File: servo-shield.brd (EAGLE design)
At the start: 65 x 56 mm, 30 parts, among them IC1 24AA01P, K1 PIN20X2

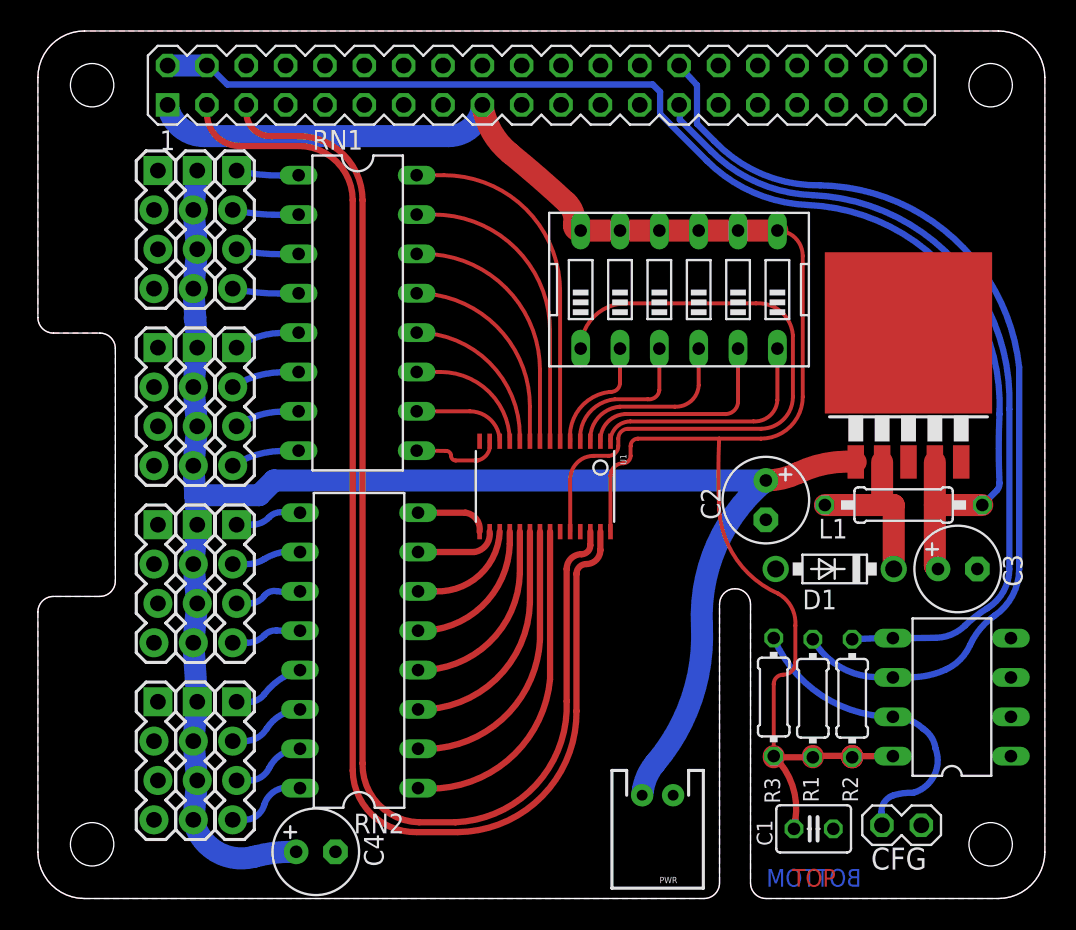
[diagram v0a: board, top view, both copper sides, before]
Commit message: Mk2 board. Move servo connectors to longer edge, remove HAT related crap. We're not using it anyway, its just i2c. Fixed issues with regulator using a bogus inductor. Fixed power connector. Hopefully fixed clearance issues with standoffs. Fixed clearance issue with soldering 40 pin connector hitting previous resistor networks. Use more SMD parts to reduce PCB used space. This WILL require a stencil.
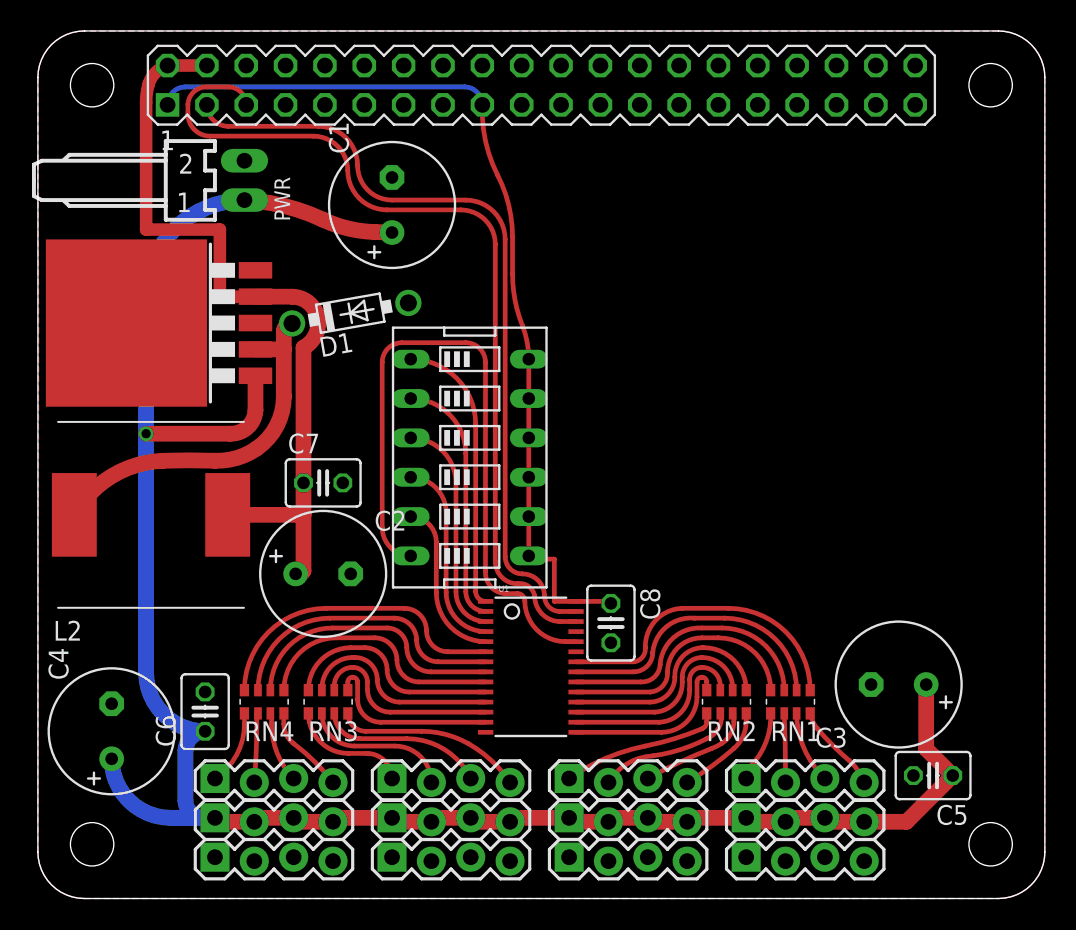
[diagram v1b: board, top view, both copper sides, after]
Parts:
- removed CFG: (no value), FLYFISH:PIN_W_2
- removed IC1: 24AA01P, microchip:DIL8
- removed L1: 33uh, rcl:0207/10
- removed R1, R2: 3k9, rcl:0204/7
- removed R3: 1k, rcl:0204/7
- added C5, C6, C7, C8: 100nf, rcl:C025-030X050
- added L2: 33uh, WE-PD:WE-PD_1260/1245/1280/1210
- added RN3, RN4: (no value), resistor-dil:EXB38V
- C1: value 100nF -> 1000uf; device rcl:C025-030X050 -> rcl:E3,5-8
- C2: value 680uf -> 1000uf; device rcl:E2,5-6 -> rcl:E3,5-8
- C3: value 220uf -> 1000uf; device rcl:E2,5-6 -> rcl:E3,5-8
- C4: value 640uf -> 1000uf; device rcl:E2,5-6 -> rcl:E3,5-8
- PWR: value (none) -> 22-05-7028-02; device SparkFun-Connectors:JST-2-PTH -> con-molex:7395-02
- RN1, RN2: device resistor-dil:DIL16 -> resistor-dil:EXB38V
- moved C1 48.6 mm to (22.9, 44.8), turned to 90 degrees
- moved IC2 48.0 mm to (8.26, 37.1), turned to 90 degrees
- moved PWR 47.8 mm to (13.3, 46.4), turned to 270 degrees
- moved JP9 44.6 mm to (11.4, 2.54), turned to 0 degrees
- moved JP5 41.9 mm to (11.4, 5.08), turned to 0 degrees
- moved JP12 39.4 mm to (45.7, 2.54), turned to 0 degrees
- moved JP1 39.4 mm to (11.4, 7.62), turned to 0 degrees
- moved RN1 37.6 mm to (48.6, 12.7), turned to 180 degrees
- moved JP10 36.4 mm to (22.9, 2.54), turned to 0 degrees
- moved JP8 36.4 mm to (45.7, 5.08), turned to 0 degrees
- moved D1 35.4 mm to (20.2, 37.8), turned to 10 degrees
- moved JP11 34.3 mm to (34.3, 2.54), turned to 0 degrees
- moved JP4 33.4 mm to (45.7, 7.62), turned to 0 degrees
- moved JP6 33.0 mm to (22.9, 5.08), turned to 0 degrees
- moved JP7 30.7 mm to (34.3, 5.08), turned to 0 degrees
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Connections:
- removed net N$16: SW1.6, U1.1
- removed net N$40: D1.C, IC2.2, L1.1
- new net VOUT: D1.C, IC2.2, L2.1
- net +3V3: now also C8.1; no longer C1.1, IC1.8, R1.2, R2.2, R3.2
- net +5V: now also C2.+, C7.1, L2.2; no longer C3.+, L1.2
- net GND: now also C1.-, C5.2, C6.2, C7.2, C8.2, PWR.2; no longer C1.2, CFG.2, IC1.1, IC1.2, IC1.3, IC1.4, PWR.1
- net ID_SCL: no longer IC1.6, R1.1
- net ID_SDA: no longer IC1.5, R2.1
- net N$1: now also RN2.3; no longer RN2.7
- net N$10: now also RN2.6; no longer RN2.10
- net N$11: now also U1.1; no longer U1.24
- net N$12: now also U1.2; no longer U1.5
- net N$13: now also SW1.5, U1.5; no longer SW1.3, U1.4
- net N$14: now also SW1.3; no longer SW1.4
- net N$15: now also SW1.4, U1.4; no longer SW1.5, U1.2
- net N$17: now also RN2.7; no longer RN2.11
- net N$18: now also RN2.8; no longer RN2.12
- net N$19: now also RN1.5; no longer RN2.13
- net N$2: now also RN2.4; no longer RN2.8
- net N$20: now also RN1.6; no longer RN2.14
- net N$21: now also RN1.7; no longer RN2.15
- net N$22: now also RN1.8; no longer RN2.16
- net N$23: now also RN1.1; no longer RN2.1
- net N$24: now also RN1.2; no longer RN2.2
- net N$25: now also RN1.3; no longer RN2.3
- net N$26: now also RN1.4; no longer RN2.4
- net N$27: now also RN2.1; no longer RN2.5
- net N$28: now also RN2.2; no longer RN2.6
- net N$29: now also RN3.2; no longer RN1.10
- net N$3: now also RN3.1; no longer RN1.9
- net N$30: now also RN3.3; no longer RN1.11
- net N$31: now also RN3.4; no longer RN1.12
- net N$32: now also RN4.1; no longer RN1.13
- net N$33: now also RN4.2; no longer RN1.14
- net N$34: now also RN4.3; no longer RN1.15
- net N$35: now also RN4.4; no longer RN1.16
- net N$36: now also RN3.5; no longer RN1.5
- net N$37: now also RN3.8; no longer RN1.8
- net N$38: now also RN3.7; no longer RN1.7
- net N$39: now also RN3.6; no longer RN1.6
- net N$4: now also SW1.6, U1.24; no longer CFG.1, IC1.7, R3.1
- net N$5: now also RN4.8; no longer RN1.4
- net N$6: now also RN4.7; no longer RN1.3
- net N$7: now also RN4.6; no longer RN1.2
- net N$8: now also RN4.5; no longer RN1.1
- net N$9: now also RN2.5; no longer RN2.9
- net V+: now also C1.+, C3.+, C5.1, C6.1, PWR.1; no longer C2.+, PWR.2
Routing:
- net ID_SCL: track 61.0 -> 0.00 mm
- net ID_SDA: track 52.2 -> 0.00 mm
- net +3V3: track 110.5 -> 59.1 mm
- net I2C_SDA: track 80.7 -> 49.4 mm
- net +5V: track 80.0 -> 51.5 mm
- net VOUT: track 0.00 -> 23.4 mm
- net N$4: track 19.5 -> 42.2 mm
- net N$11: track 39.9 -> 17.6 mm
- net I2C_SCL: track 76.5 -> 55.8 mm
- net V+: track 114.5 -> 130.9 mm, vias 0 -> 1
- net N$16: track 15.2 -> 0.00 mm
- net N$40: track 11.4 -> 0.00 mm
- net N$12: track 7.20 -> 15.7 mm
- net N$37: track 4.40 -> 12.0 mm
- net N$1: track 5.27 -> 12.0 mm
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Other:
- outline, holes or cut-outs redrawn
- board text removed: "BOTTOM"
- board text removed: "TOP"

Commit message: Move some parts labels about
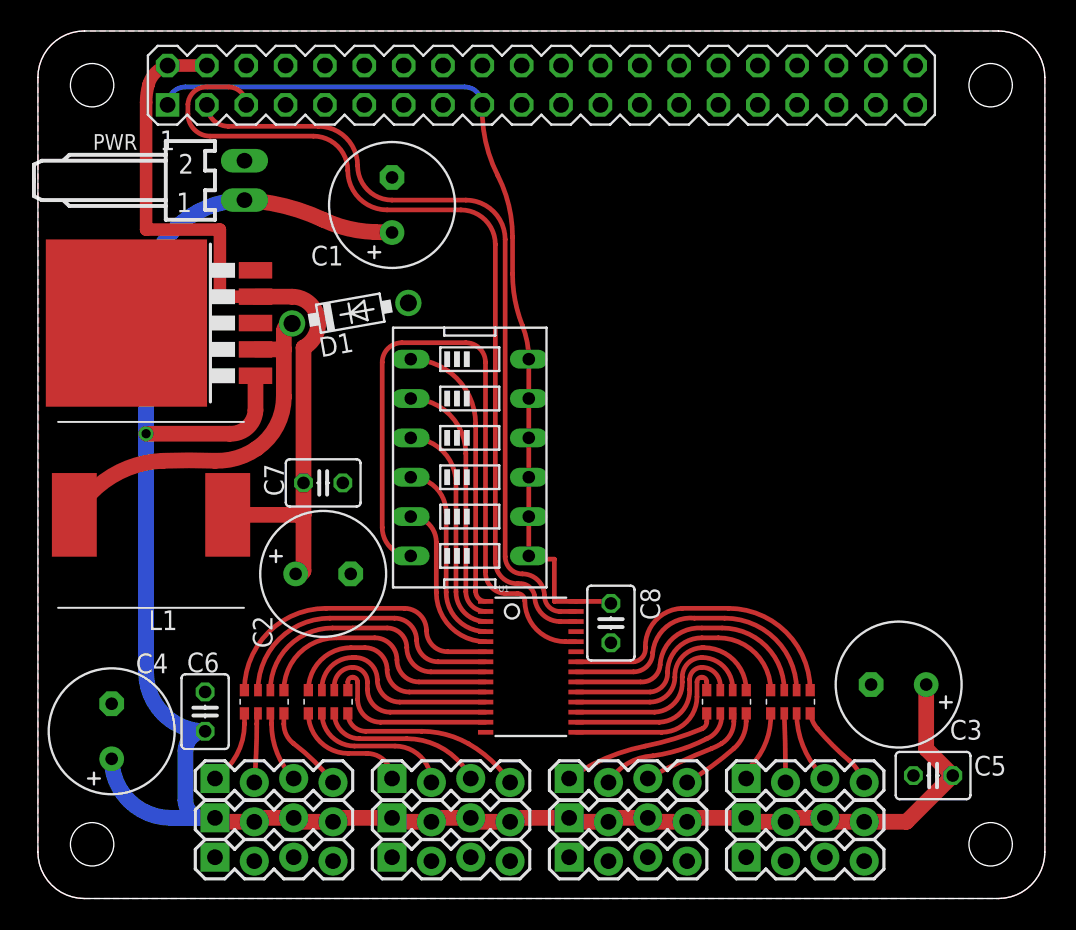
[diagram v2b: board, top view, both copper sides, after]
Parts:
- renumbered L2 to L1
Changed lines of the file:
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@@
 <attribute name="VALUE" x="18.667346875" y="34.553021875" size="1.27" layer="27" ratio="10" rot="R10"/>
 </element>
-<element name="L2" library="WE-PD" package="WE-PD_1260/1245/1280/1210" value="33uh" x="7.3025" y="24.765">
+<element name="L1" library="WE-PD" package="WE-PD_1260/1245/1280/1210" value="33uh" x="7.3025" y="24.765" smashed="yes">
 <attribute name="PACKAGE" value="1280" x="7.3025" y="24.765" size="1.778" layer="27" display="off"/>
 <attribute name="OC_NEWARK" value="88T7068" x="7.3025" y="24.765" size="1.778" layer="27" display="off"/>
@@
 <attribute name="SUPPLIER" value="Wuerth Elektronik" x="7.3025" y="24.765" size="1.778" layer="27" display="off"/>
 <attribute name="OC_FARNELL" value="2082596" x="7.3025" y="24.765" size="1.778" layer="27" display="off"/>
-</element>
-<element name="C2" library="rcl" package="E3,5-8" value="1000uf" x="18.415" y="20.955"/>
-<element name="C3" library="rcl" package="E3,5-8" value="1000uf" x="55.5625" y="13.81125" rot="R180"/>
-<element name="C5" library="rcl" package="C025-030X050" value="100nf" x="57.785" y="7.9375" rot="R180"/>
-<element name="C7" library="rcl" package="C025-030X050" value="100nf" x="18.415" y="26.82875"/>
-<element name="C1" library="rcl" package="E3,5-8" value="1000uf" x="22.86" y="44.7675" rot="R90"/>
-<element name="C8" library="rcl" package="C025-030X050" value="100nf" x="36.98875" y="17.78" rot="R270"/>
-<element name="RN1" library="resistor-dil" package="EXB38V" value="" x="48.5775" y="12.7" rot="R180">
+<attribute name="NAME" x="9.00875" y="18.5975" size="1.27" layer="25" rot="R180"/>
+<attribute name="VALUE" x="1.4925" y="32.115" size="1.27" layer="27"/>
+</element>
+<element name="C2" library="rcl" package="E3,5-8" value="1000uf" x="18.415" y="20.955" smashed="yes">
+<attribute name="NAME" x="15.14475" y="16.16075" size="1.27" layer="25" ratio="10" rot="R90"/>
+<attribute name="VALUE" x="16.129" y="17.907" size="1.27" layer="27" ratio="10"/>
+</element>
+<element name="C3" library="rcl" package="E3,5-8" value="1000uf" x="55.5625" y="13.81125" smashed="yes" rot="R180">
+<attribute name="NAME" x="58.8645" y="10.25525" size="1.27" layer="25" ratio="10"/>
+<attribute name="VALUE" x="57.8485" y="16.85925" size="1.27" layer="27" ratio="10" rot="R180"/>
+</element>
+<element name="C5" library="rcl" package="C025-030X050" value="100nf" x="57.785" y="7.9375" smashed="yes" rot="R180">
+<attribute name="NAME" x="60.42025" y="7.9375" size="1.27" layer="25" ratio="10"/>
+<attribute name="VALUE" x="60.071" y="10.9855" size="1.27" layer="27" ratio="10" rot="R180"/>
+</element>
+<element name="C7" library="rcl" package="C025-030X050" value="100nf" x="18.415" y="26.82875" smashed="yes">
+<attribute name="NAME" x="15.875" y="25.9715" size="1.27" layer="25" ratio="10" rot="R90"/>
+<attribute name="VALUE" x="16.129" y="23.78075" size="1.27" layer="27" ratio="10"/>
+</element>
+<element name="C1" library="rcl" package="E3,5-8" value="1000uf" x="22.86" y="44.7675" smashed="yes" rot="R90">
+<attribute name="NAME" x="19.71675" y="42.13225" size="1.27" layer="25" ratio="10" rot="R180"/>
+<attribute name="VALUE" x="25.908" y="42.4815" size="1.27" layer="27" ratio="10" rot="R90"/>
+</element>
+<element name="C8" library="rcl" package="C025-030X050" value="100nf" x="36.98875" y="17.78" smashed="yes" rot="R270">
+<attribute name="NAME" x="38.89375" y="20.066" size="1.27" layer="25" ratio="10" rot="R270"/>
+<attribute name="VALUE" x="33.94075" y="20.066" size="1.27" layer="27" ratio="10" rot="R270"/>
+</element>
+<element name="RN1" library="resistor-dil" package="EXB38V" value="" x="48.5775" y="12.7" smashed="yes" rot="R180">
 <attribute name="OC_NEWARK" value="unknown" x="48.5775" y="12.7" size="1.778" layer="27" rot="R180" display="off"/>
 <attribute name="MPN" value="" x="48.5775" y="12.7" size="1.778" layer="27" rot="R180" display="off"/>
 <attribute name="MF" value="" x="48.5775" y="12.7" size="1.778" layer="27" rot="R180" display="off"/>
 <attribute name="OC_FARNELL" value="unknown" x="48.5775" y="12.7" size="1.778" layer="27" rot="R180" display="off"/>
-</element>
-<element name="RN2" library="resistor-dil" package="EXB38V" value="" x="44.45" y="12.7" rot="R180">
+<attribute name="VALUE" x="50.55" y="15.24" size="1.27" layer="27" rot="R180"/>
+</element>
+<element name="RN2" library="resistor-dil" package="EXB38V" value="" x="44.45" y="12.7" smashed="yes" rot="R180">
 <attribute name="OC_NEWARK" value="unknown" x="44.45" y="12.7" size="1.778" layer="27" rot="R180" display="off"/>
 <attribute name="MPN" value="" x="44.45" y="12.7" size="1.778" layer="27" rot="R180" display="off"/>
 <attribute name="MF" value="" x="44.45" y="12.7" size="1.778" layer="27" rot="R180" display="off"/>
 <attribute name="OC_FARNELL" value="unknown" x="44.45" y="12.7" size="1.778" layer="27" rot="R180" display="off"/>
-</element>
-<element name="RN3" library="resistor-dil" package="EXB38V" value="" x="18.7325" y="12.7" rot="R180">
+<attribute name="VALUE" x="46.4225" y="15.24" size="1.27" layer="27" rot="R180"/>
+</element>
+<element name="RN3" library="resistor-dil" package="EXB38V" value="" x="18.7325" y="12.7" smashed="yes" rot="R180">
 <attribute name="OC_NEWARK" value="unknown" x="18.7325" y="12.7" size="1.778" layer="27" rot="R180" display="off"/>
 <attribute name="MPN" value="" x="18.7325" y="12.7" size="1.778" layer="27" rot="R180" display="off"/>
 <attribute name="MF" value="" x="18.7325" y="12.7" size="1.778" layer="27" rot="R180" display="off"/>
 <attribute name="OC_FARNELL" value="unknown" x="18.7325" y="12.7" size="1.778" layer="27" rot="R180" display="off"/>
-</element>
-<element name="RN4" library="resistor-dil" package="EXB38V" value="" x="14.605" y="12.7" rot="R180">
+<attribute name="VALUE" x="20.705" y="15.24" size="1.27" layer="27" rot="R180"/>
+</element>
+<element name="RN4" library="resistor-dil" package="EXB38V" value="" x="14.605" y="12.7" smashed="yes" rot="R180">
 <attribute name="OC_NEWARK" value="unknown" x="14.605" y="12.7" size="1.778" layer="27" rot="R180" display="off"/>
 <attribute name="MPN" value="" x="14.605" y="12.7" size="1.778" layer="27" rot="R180" display="off"/>
 <attribute name="MF" value="" x="14.605" y="12.7" size="1.778" layer="27" rot="R180" display="off"/>
 <attribute name="OC_FARNELL" value="unknown" x="14.605" y="12.7" size="1.778" layer="27" rot="R180" display="off"/>
-</element>
-<element name="PWR" library="con-molex" package="7395-02" value="22-05-7028-02" x="13.335" y="46.355" rot="R270">
+<attribute name="VALUE" x="16.5775" y="15.24" size="1.27" layer="27" rot="R180"/>
+</element>
+<element name="PWR" library="con-molex" package="7395-02" value="22-05-7028-02" x="13.335" y="46.355" smashed="yes" rot="R270">
 <attribute name="OC_NEWARK" value="unknown" x="13.335" y="46.355" size="1.778" layer="27" rot="R270" display="off"/>
 <attribute name="MPN" value="" x="13.335" y="46.355" size="1.778" layer="27" rot="R270" display="off"/>
 <attribute name="MF" value="" x="13.335" y="46.355" size="1.778" layer="27" rot="R270" display="off"/>
 <attribute name="OC_FARNELL" value="9731601" x="13.335" y="46.355" size="1.778" layer="27" rot="R270" display="off"/>
-</element>
-<element name="C4" library="rcl" package="E3,5-8" value="1000uf" x="4.7625" y="10.795" rot="R90"/>
-<element name="C6" library="rcl" package="C025-030X050" value="100nf" x="10.795" y="12.065" rot="R90"/>
+<attribute name="NAME" x="3.55115" y="48.32835" size="1.016" layer="25" ratio="10"/>
+<attribute name="VALUE" x="10.8951" y="42.9529" size="0.8128" layer="27" ratio="10" rot="R180"/>
+</element>
+<element name="C4" library="rcl" package="E3,5-8" value="1000uf" x="4.7625" y="10.795" smashed="yes" rot="R90">
+<attribute name="NAME" x="6.31825" y="14.5415" size="1.27" layer="25" ratio="10"/>
+<attribute name="VALUE" x="7.8105" y="8.509" size="1.27" layer="27" ratio="10" rot="R90"/>
+</element>
+<element name="C6" library="rcl" package="C025-030X050" value="100nf" x="10.795" y="12.065" smashed="yes" rot="R90">
+<attribute name="NAME" x="9.62025" y="14.605" size="1.27" layer="25" ratio="10"/>
+<attribute name="VALUE" x="13.843" y="9.779" size="1.27" layer="27" ratio="10" rot="R90"/>
+</element>
 </elements>
 <signals>
@@
 <contactref element="K1" pad="4"/>
 <contactref element="IC2" pad="4"/>
-<contactref element="L2" pad="2"/>
+<contactref element="L1" pad="2"/>
 <contactref element="C2" pad="+"/>
 <contactref element="C7" pad="1"/>
@@
 <contactref element="IC2" pad="2"/>
 <contactref element="D1" pad="C"/>
-<contactref element="L2" pad="1"/>
+<contactref element="L1" pad="1"/>
 <wire x1="14.0462" y1="35.4457" x2="15.875" y2="35.4457" width="1.016" layer="1"/>
 <wire x1="15.875" y1="35.4457" x2="15.875" y2="32.385" width="1.016" layer="1"/>
